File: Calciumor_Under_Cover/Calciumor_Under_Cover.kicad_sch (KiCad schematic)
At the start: 35 parts, among them J1 NeoPixel

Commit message: Core_rev1.0
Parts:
- removed D1, D10, D11, D12, D13, D14, D15, D16, D17, D18, D19, D2, D20, D21, D22, D23, D24, D25, D26, D27, D28, D29, D3, D30, D31, D32, D34, D35, D4, D5, D6, D7, D8, D9: WS2812B, LED_SMD:LED_WS2812B_PLCC4_5.0x5.0mm_P3.2mm, symbol LED:WS2812B
- added D1, D10, D11, D12, D13, D14, D15, D16, D17, D18, D19, D2, D20, D21, D22, D23, D24, D25, D26, D27, D28, D29, D3, D30, D31, D32, D33, D34, D4, D5, D6, D7, D8, D9: SK6812MINI, LED_SMD:LED_SK6812MINI_PLCC4_3.5x3.5mm_P1.75mm, symbol LED:SK6812MINI
- added D35, D36, D37, D38, D39, D40, D41, D42, D43, D44, D45, D46, D47, D48, D49, D50, D51, D52, D53, D54, D55, D56, D57, D58, D59, D60, D61, D62, D63, D64, D65, D66, D67, D68, D69, D70, D71, D72, D73, D74, D75, D76, D77, D78, D79, D80, D81, D82, D83, D84: LED, LED_SMD:LED_0603_1608Metric, symbol Device:LED
- added J2: NeoPixel, Connector_JST:JST_PH_S4B-PH-SM4-TB_1x04-1MP_P2.00mm_Horizontal, symbol Connector:Conn_01x05_Socket
- added R1: 470, Resistor_SMD:R_1206_3216Metric, symbol Device:R
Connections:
- net +5V: now also D1.4 (VDD), D10.4 (VDD), D11.4 (VDD), D12.4 (VDD), D13.4 (VDD), D14.4 (VDD), D15.4 (VDD), D16.4 (VDD), D17.4 (VDD), D18.4 (VDD), D19.4 (VDD), D2.4 (VDD), D20.4 (VDD), D21.4 (VDD), D22.4 (VDD), D23.4 (VDD), D24.4 (VDD), D25.4 (VDD), D26.4 (VDD), D27.4 (VDD), D28.4 (VDD), D29.4 (VDD), D3.4 (VDD), D30.4 (VDD), D31.4 (VDD), D32.4 (VDD), D33.4 (VDD), D34.4 (VDD), D4.4 (VDD), D5.4 (VDD), D6.4 (VDD), D7.4 (VDD), D8.4 (VDD), D9.4 (VDD), J2.2 (Pin_2)
- net GND: now also D1.2 (VSS), D10.2 (VSS), D11.2 (VSS), D12.2 (VSS), D13.2 (VSS), D14.2 (VSS), D15.2 (VSS), D16.2 (VSS), D17.2 (VSS), D18.2 (VSS), D19.2 (VSS), D2.2 (VSS), D20.2 (VSS), D21.2 (VSS), D22.2 (VSS), D23.2 (VSS), D24.2 (VSS), D25.2 (VSS), D26.2 (VSS), D27.2 (VSS), D28.2 (VSS), D29.2 (VSS), D3.2 (VSS), D30.2 (VSS), D31.2 (VSS), D32.2 (VSS), D33.2 (VSS), D34.2 (VSS), D4.2 (VSS), D5.2 (VSS), D6.2 (VSS), D7.2 (VSS), D8.2 (VSS), D9.2 (VSS), J2.3 (Pin_3), J2.MP (Pin_5), R1.2
- net LED: now also D35.2 (A), D36.2 (A), D37.2 (A), D38.2 (A), D39.2 (A), D40.2 (A), D41.2 (A), D42.2 (A), D43.2 (A), D44.2 (A), D45.2 (A), D46.2 (A), D47.2 (A), D48.2 (A), D49.2 (A), D50.2 (A), D51.2 (A), D52.2 (A), D53.2 (A), D54.2 (A), D55.2 (A), D56.2 (A), D57.2 (A), D58.2 (A), D59.2 (A), D60.2 (A), D61.2 (A), D62.2 (A), D63.2 (A), D64.2 (A), D65.2 (A), D66.2 (A), D67.2 (A), D68.2 (A), D69.2 (A), D70.2 (A), D71.2 (A), D72.2 (A), D73.2 (A), D74.2 (A), D75.2 (A), D76.2 (A), D77.2 (A), D78.2 (A), D79.2 (A), D80.2 (A), D81.2 (A), D82.2 (A), D83.2 (A), D84.2 (A), J2.4 (Pin_4)
- net RGB: now also D1.3 (DIN), D5.3 (DIN), J2.1 (Pin_1)
- new net: D5.1 (DOUT), D6.3 (DIN)
- new net: D3.1 (DOUT), D4.3 (DIN)
- new net: D12.3 (DIN), D13.1 (DOUT)
- new net: D1.1 (DOUT), D2.3 (DIN)
- new net: D11.1 (DOUT), D15.3 (DIN)
- new net: D21.1 (DOUT), D22.3 (DIN)
- new net: D20.1 (DOUT), D21.3 (DIN)
- new net: D25.1 (DOUT), D29.3 (DIN)
- new net: D10.1 (DOUT), D11.3 (DIN)
- new net: D31.1 (DOUT), D32.3 (DIN)
- new net: D33.1 (DOUT), D34.3 (DIN)
- new net: D17.3 (DIN), D18.1 (DOUT)
- new net: D18.3 (DIN), D19.1 (DOUT)
- new net: D13.3 (DIN), D14.1 (DOUT)
- new net: D26.3 (DIN), D27.1 (DOUT)
- new net: D27.3 (DIN), D28.1 (DOUT)
- new net: D2.1 (DOUT), D3.3 (DIN)
- new net: D7.1 (DOUT), D8.3 (DIN)
- new net: D6.1 (DOUT), D7.3 (DIN)
- new net: D24.1 (DOUT), D25.3 (DIN)
- new net D10: D22.1 (DOUT), D23.3 (DIN), D29.1 (DOUT), D30.3 (DIN)
- new net D11: D19.3 (DIN), D23.1 (DOUT), D28.3 (DIN), D30.1 (DOUT)
- new net D14: D17.1 (DOUT), D26.1 (DOUT), D31.3 (DIN), D33.3 (DIN)
- new net D3: D16.3 (DIN), D4.1 (DOUT), D8.1 (DOUT), D9.3 (DIN)
- new net D4: D10.3 (DIN), D14.3 (DIN), D16.1 (DOUT), D9.1 (DOUT)
- new net D7: D12.1 (DOUT), D15.1 (DOUT), D20.3 (DIN), D24.3 (DIN)
- new net LED_R: D35.1 (K), D36.1 (K), D37.1 (K), D38.1 (K), D39.1 (K), D40.1 (K), D41.1 (K), D42.1 (K), D43.1 (K), D44.1 (K), D45.1 (K), D46.1 (K), D47.1 (K), D48.1 (K), D49.1 (K), D50.1 (K), D51.1 (K), D52.1 (K), D53.1 (K), D54.1 (K), D55.1 (K), D56.1 (K), D57.1 (K), D58.1 (K), D59.1 (K), D60.1 (K), D61.1 (K), D62.1 (K), D63.1 (K), D64.1 (K), D65.1 (K), D66.1 (K), D67.1 (K), D68.1 (K), D69.1 (K), D70.1 (K), D71.1 (K), D72.1 (K), D73.1 (K), D74.1 (K), D75.1 (K), D76.1 (K), D77.1 (K), D78.1 (K), D79.1 (K), D80.1 (K), D81.1 (K), D82.1 (K), D83.1 (K), D84.1 (K), R1.1

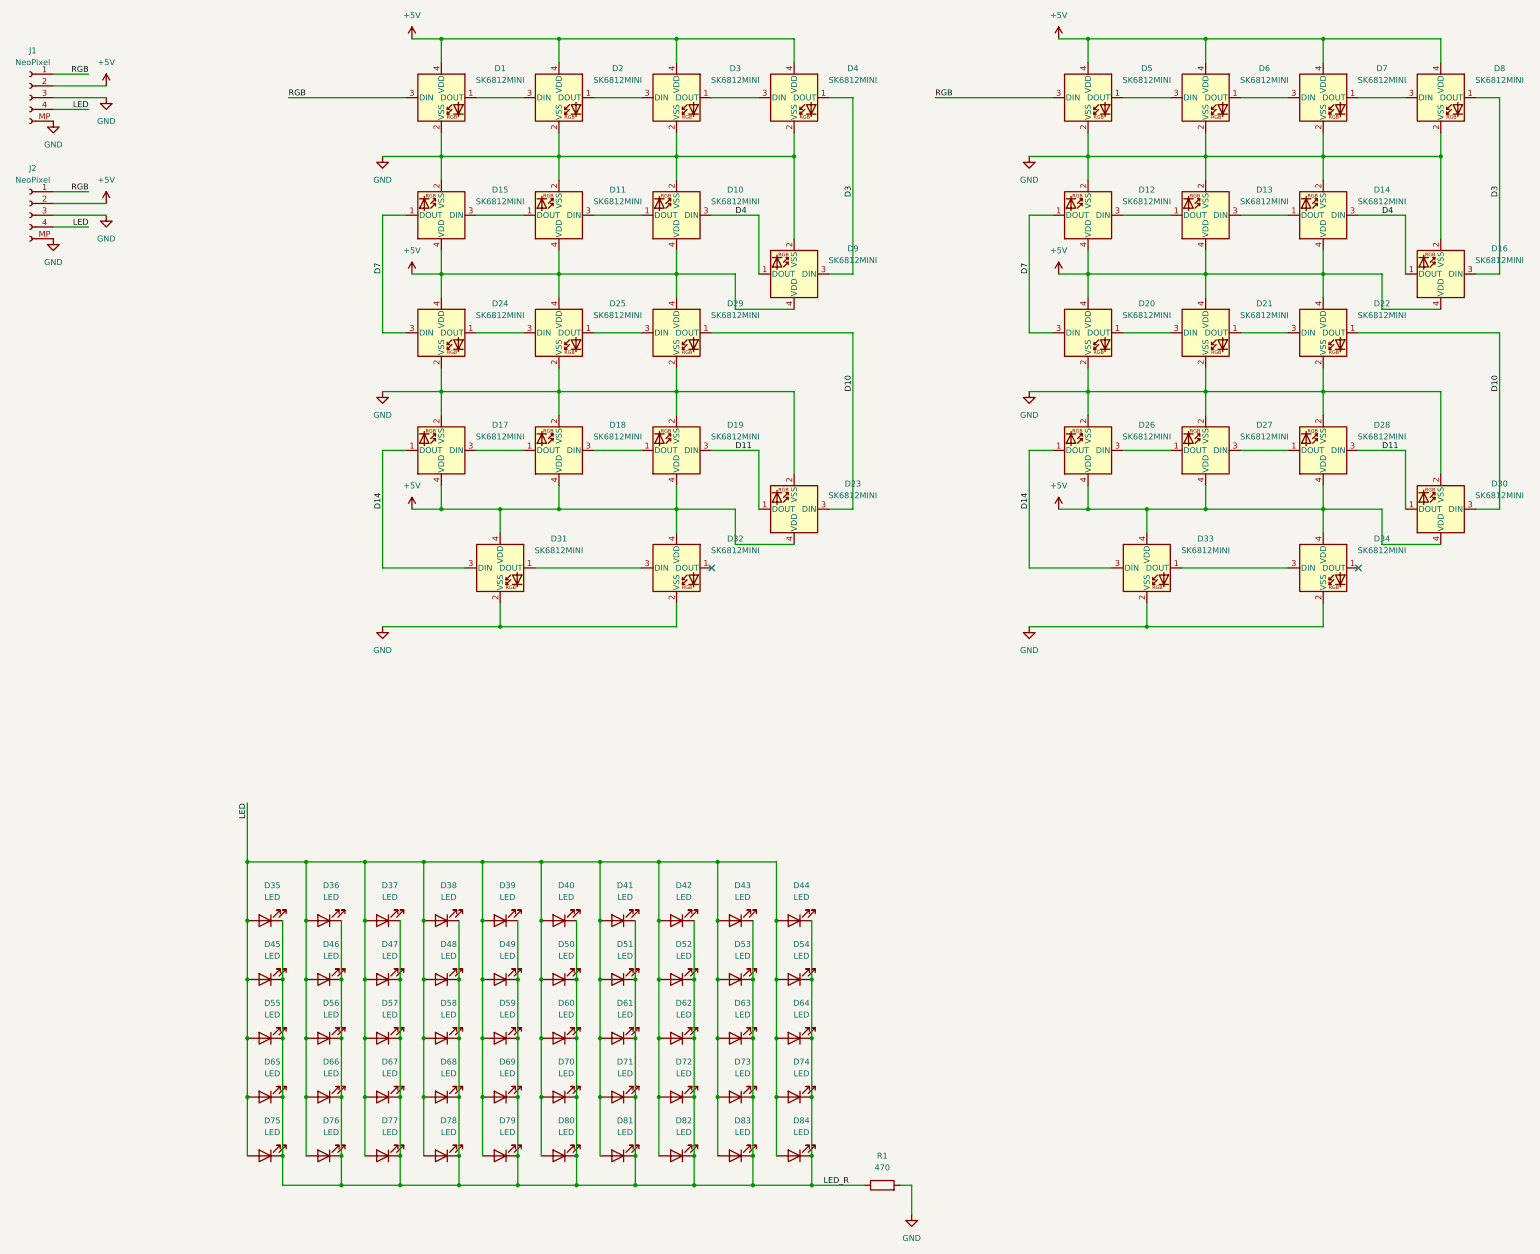
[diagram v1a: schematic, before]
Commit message: Under cover completed
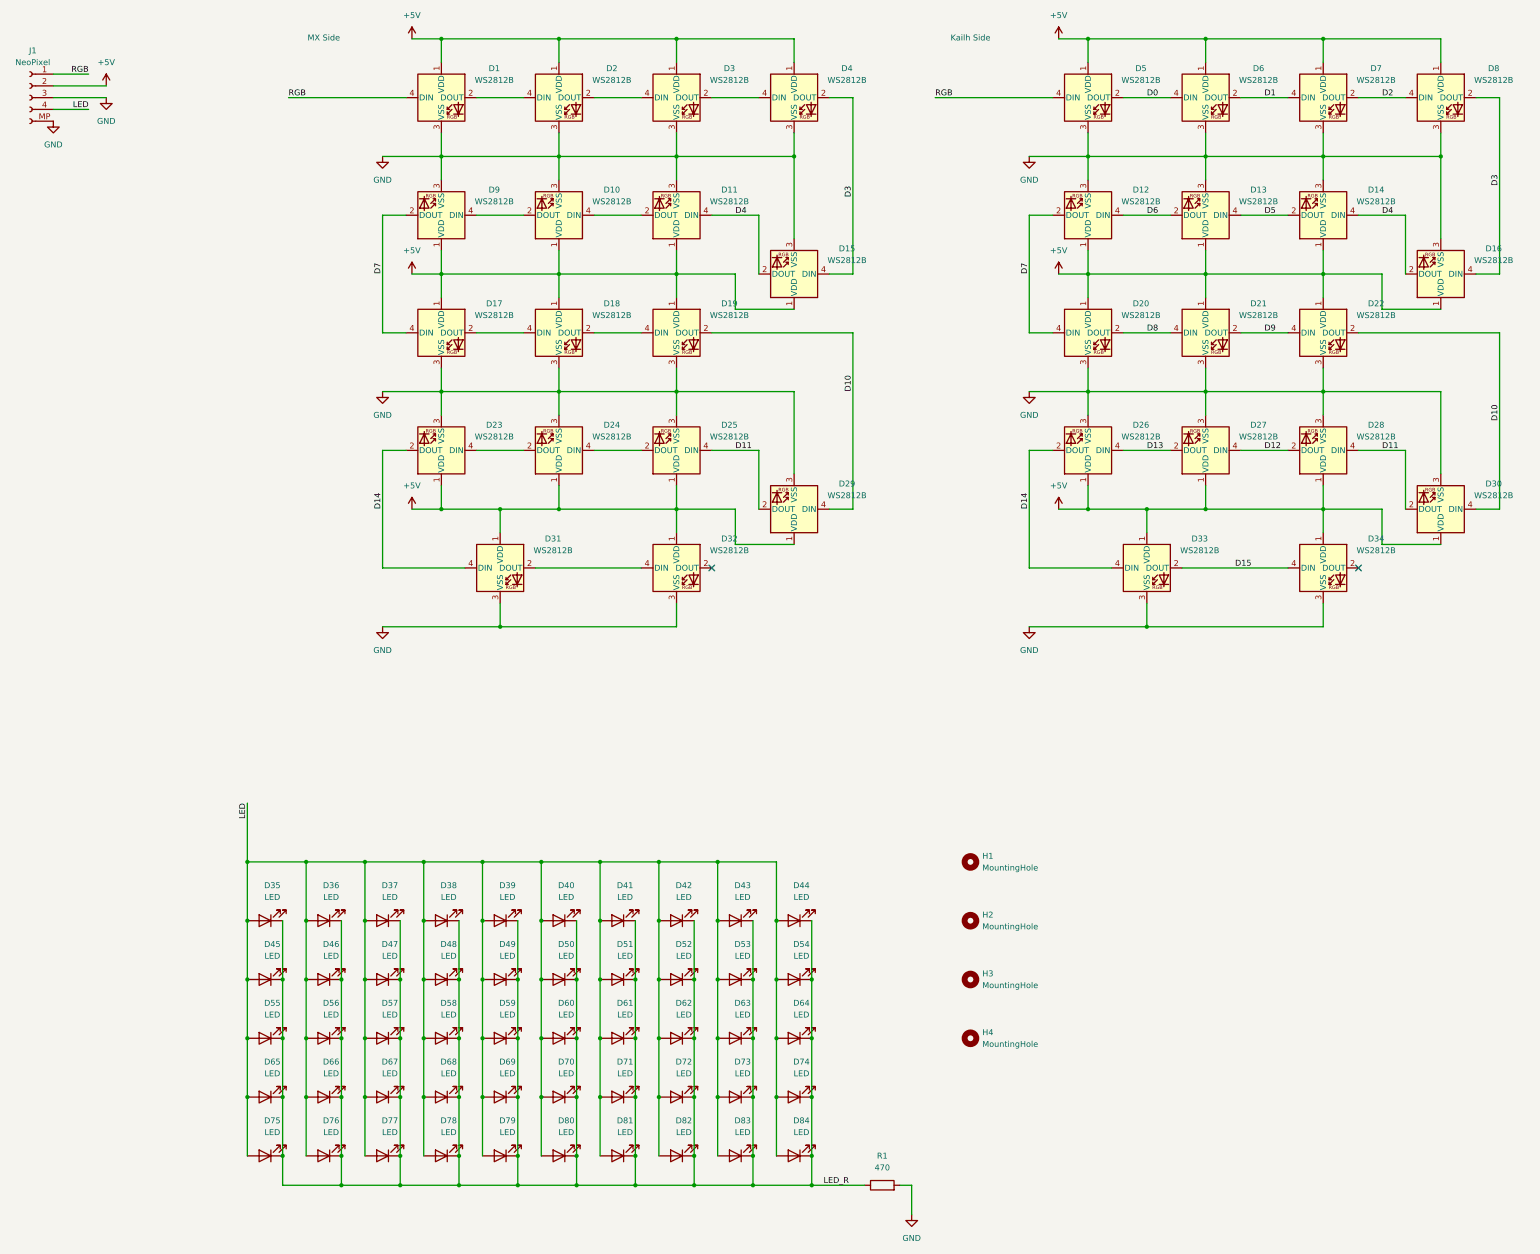
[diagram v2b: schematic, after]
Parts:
- removed D1, D10, D11, D12, D13, D14, D15, D16, D17, D18, D19, D2, D20, D21, D22, D23, D24, D25, D26, D27, D28, D29, D3, D30, D31, D32, D33, D34, D4, D5, D6, D7, D8, D9: SK6812MINI, LED_SMD:LED_SK6812MINI_PLCC4_3.5x3.5mm_P1.75mm, symbol LED:SK6812MINI
- removed J2: NeoPixel, Connector_JST:JST_PH_S4B-PH-SM4-TB_1x04-1MP_P2.00mm_Horizontal, symbol Connector:Conn_01x05_Socket
- added D1, D10, D11, D12, D13, D14, D15, D16, D17, D18, D19, D2, D20, D21, D22, D23, D24, D25, D26, D27, D28, D29, D3, D30, D31, D32, D33, D34, D4, D5, D6, D7, D8, D9: WS2812B, LED_SMD:LED_WS2812B_PLCC4_5.0x5.0mm_P3.2mm, symbol LED:WS2812B
- added H1, H2, H3, H4: MountingHole, MountingHole:MountingHole_2.2mm_M2, symbol Mechanical:MountingHole
- D35, D36, D37, D38, D39, D40, D41, D42, D43, D44, D45, D46, D47, D48, D49, D50, D51, D52, D53, D54, D55, D56, D57, D58, D59, D60, D61, D62, D63, D64, D65, D66, D67, D68, D69, D70, D71, D72, D73, D74, D75, D76, D77, D78, D79, D80, D81, D82, D83, D84: LCSC (none) -> C2290
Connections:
- net +5V: now also D1.1 (VDD), D10.1 (VDD), D11.1 (VDD), D12.1 (VDD), D13.1 (VDD), D14.1 (VDD), D15.1 (VDD), D16.1 (VDD), D17.1 (VDD), D18.1 (VDD), D19.1 (VDD), D2.1 (VDD), D20.1 (VDD), D21.1 (VDD), D22.1 (VDD), D23.1 (VDD), D24.1 (VDD), D25.1 (VDD), D26.1 (VDD), D27.1 (VDD), D28.1 (VDD), D29.1 (VDD), D3.1 (VDD), D30.1 (VDD), D31.1 (VDD), D32.1 (VDD), D33.1 (VDD), D34.1 (VDD), D4.1 (VDD), D5.1 (VDD), D6.1 (VDD), D7.1 (VDD), D8.1 (VDD), D9.1 (VDD)
- net D10: now also D19.2 (DOUT), D22.2 (DOUT), D29.4 (DIN), D30.4 (DIN)
- net D11: now also D25.4 (DIN), D28.4 (DIN), D29.2 (DOUT), D30.2 (DOUT)
- net D14: now also D23.2 (DOUT), D26.2 (DOUT), D31.4 (DIN), D33.4 (DIN)
- net D3: now also D15.4 (DIN), D16.4 (DIN), D4.2 (DOUT), D8.2 (DOUT)
- net D4: now also D11.4 (DIN), D14.4 (DIN), D15.2 (DOUT), D16.2 (DOUT)
- net D7: now also D12.2 (DOUT), D17.4 (DIN), D20.4 (DIN), D9.2 (DOUT)
- net GND: now also D1.3 (VSS), D10.3 (VSS), D11.3 (VSS), D12.3 (VSS), D13.3 (VSS), D14.3 (VSS), D15.3 (VSS), D16.3 (VSS), D17.3 (VSS), D18.3 (VSS), D19.3 (VSS), D2.3 (VSS), D20.3 (VSS), D21.3 (VSS), D22.3 (VSS), D23.3 (VSS), D24.3 (VSS), D25.3 (VSS), D26.3 (VSS), D27.3 (VSS), D28.3 (VSS), D29.3 (VSS), D3.3 (VSS), D30.3 (VSS), D31.3 (VSS), D32.3 (VSS), D33.3 (VSS), D34.3 (VSS), D4.3 (VSS), D5.3 (VSS), D6.3 (VSS), D7.3 (VSS), D8.3 (VSS), D9.3 (VSS)
- net RGB: now also D1.4 (DIN), D5.4 (DIN)
- new net: D23.4 (DIN), D24.2 (DOUT)
- new net: D3.2 (DOUT), D4.4 (DIN)
- new net: D2.2 (DOUT), D3.4 (DIN)
- new net: D18.2 (DOUT), D19.4 (DIN)
- new net: D24.4 (DIN), D25.2 (DOUT)
- new net: D10.2 (DOUT), D9.4 (DIN)
- new net: D10.4 (DIN), D11.2 (DOUT)
- new net: D17.2 (DOUT), D18.4 (DIN)
- new net: D31.2 (DOUT), D32.4 (DIN)
- new net: D1.2 (DOUT), D2.4 (DIN)
- new net D0: D5.2 (DOUT), D6.4 (DIN)
- new net D1: D6.2 (DOUT), D7.4 (DIN)
- new net D12: D27.4 (DIN), D28.2 (DOUT)
- new net D13: D26.4 (DIN), D27.2 (DOUT)
- new net D15: D33.2 (DOUT), D34.4 (DIN)
- new net D2: D7.2 (DOUT), D8.4 (DIN)
- new net D5: D13.4 (DIN), D14.2 (DOUT)
- new net D6: D12.4 (DIN), D13.2 (DOUT)
- new net D8: D20.2 (DOUT), D21.4 (DIN)
- new net D9: D21.2 (DOUT), D22.4 (DIN)
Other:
- note added: "Kailh Side"
- note added: "MX Side"
